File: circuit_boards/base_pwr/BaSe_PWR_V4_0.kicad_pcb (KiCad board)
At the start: 4 copper layers, 114.2 x 101.5 mm, 103 parts, among them J1 12VDC In, J10 Conn_01x04_Socket, J11 MOTOR, J12 USB3_A, J3 USB_B_Micro, J4 Conn_01x07_Pin, J5 Conn_02x06_Odd_Even, J6 USB3_B_Micro, J7 Conn_02x06_Odd_Even, J8 USB_C_Receptacle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

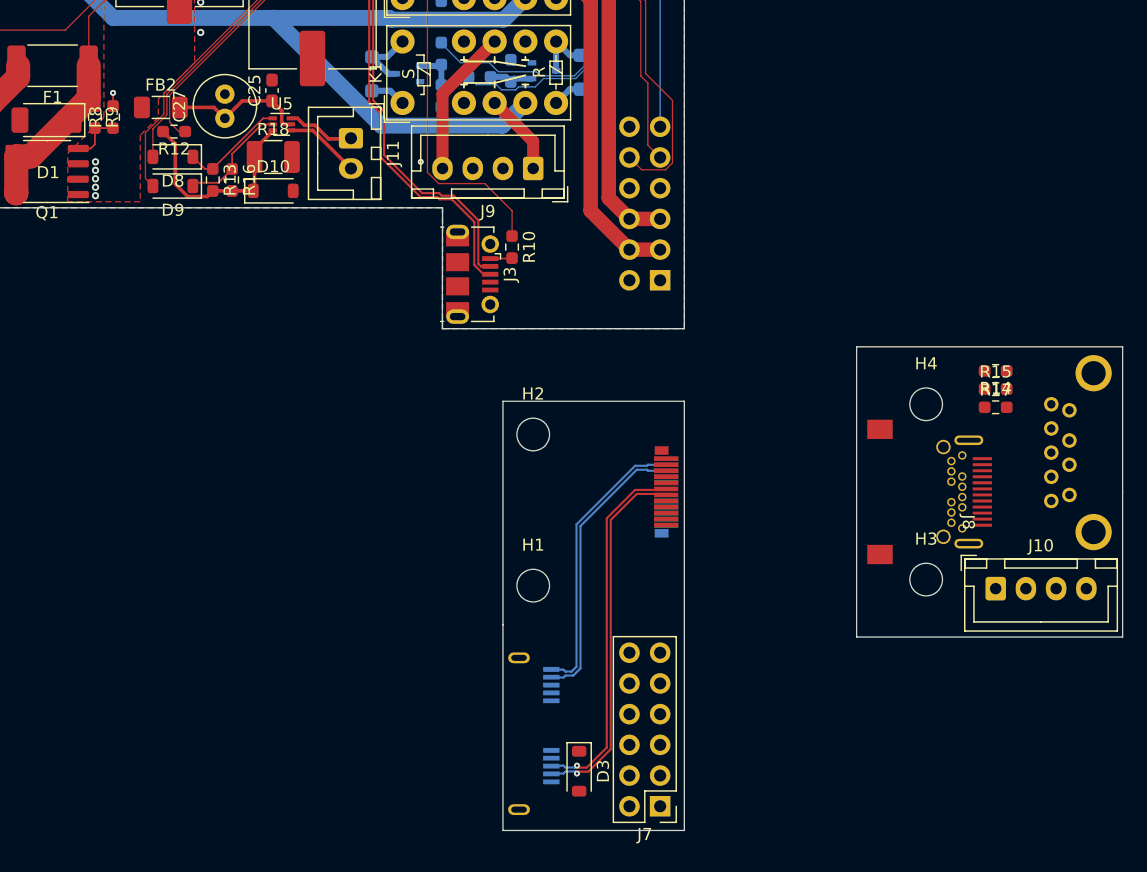
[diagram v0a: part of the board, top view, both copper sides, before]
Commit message: BaSe PWR V4.0: rotate b2b connectors 180 degree for shorter pwr tracks
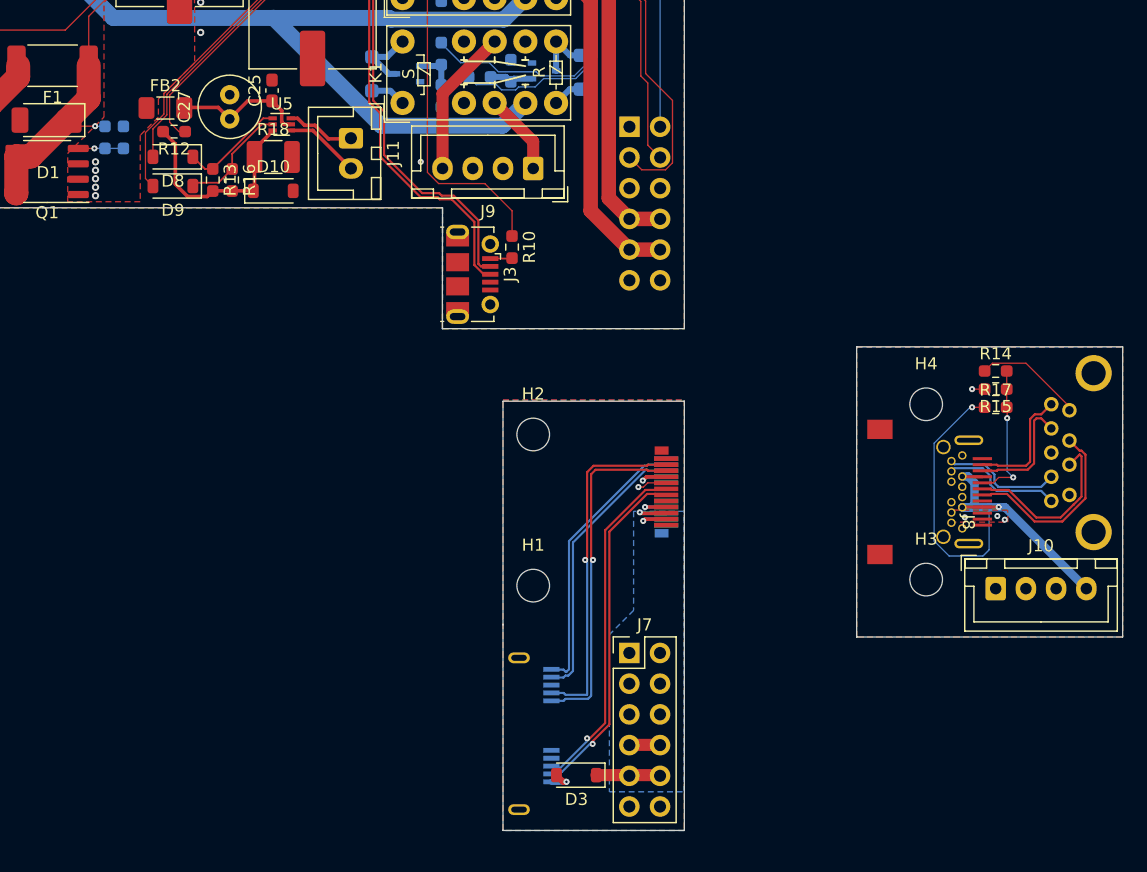
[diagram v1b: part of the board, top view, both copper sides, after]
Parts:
- R8, R9: moved to B.Cu
- moved J5 13.0 mm to (93.5, 106.8), turned to 180 degrees
- moved J7 12.9 mm to (93.5, 150.3), turned to 0 degrees
- moved R8 1.89 mm to (51.6, 107.7)
- moved R9 1.87 mm to (50.1, 107.7)
- moved C27 0.40 mm to (60.4, 106.2)
- moved D3 0.40 mm to (89.1, 160.4), turned to 180 degrees
- moved FB2 0.38 mm to (55.1, 105.2)
- turned R14 to 0 degrees
- turned R15 to 180 degrees
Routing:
- net +12VA: track 0.00 -> 44.1 mm, vias 0 -> 2
- net /stator_tx+: track 0.00 -> 28.3 mm, vias 0 -> 1
- net /stator_tx-: track 0.00 -> 28.3 mm, vias 0 -> 1
- net /lane1_d-: track 0.00 -> 15.7 mm
- net /lane1_d+: track 0.00 -> 14.6 mm
- net /+5V_HDD_: track 0.00 -> 13.7 mm, vias 0 -> 2
- net /supply_sense: track 0.00 -> 11.8 mm, vias 0 -> 2
- net /l1_tx-: track 0.00 -> 9.91 mm
- net /l1_tx+: track 0.00 -> 9.91 mm
- net /l1_rx-: track 0.00 -> 9.91 mm
- net /l1_rx+: track 0.00 -> 9.91 mm
- net +5VA: track 0.00 -> 9.07 mm, vias 0 -> 3
- net /+12V_HDD_: track 0.00 -> 8.92 mm, vias 0 -> 2
- net /DC_preprot: track 55.3 -> 59.1 mm, vias 1 -> 2
- net GND1: track 0.00 -> 2.54 mm
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- added copper zone on F.Cu, net +5VA
- added copper zone on In2.Cu, net +5VA
- added copper zone on In2.Cu, net /+12V_HDD_
- added copper zone on B.Cu, net /+5V_HDD_
- added copper zone on B.Cu, net GND1
- added copper zone on F.Cu, net GND1
- added copper zone on In1.Cu, net GND1
- added copper zone on In2.Cu, net GND1
- added copper zone on B.Cu, net GND2
- added copper zone on F.Cu, net GND2
- added copper zone on In1.Cu, net GND2
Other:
- board text added: "BaSe HW 4"

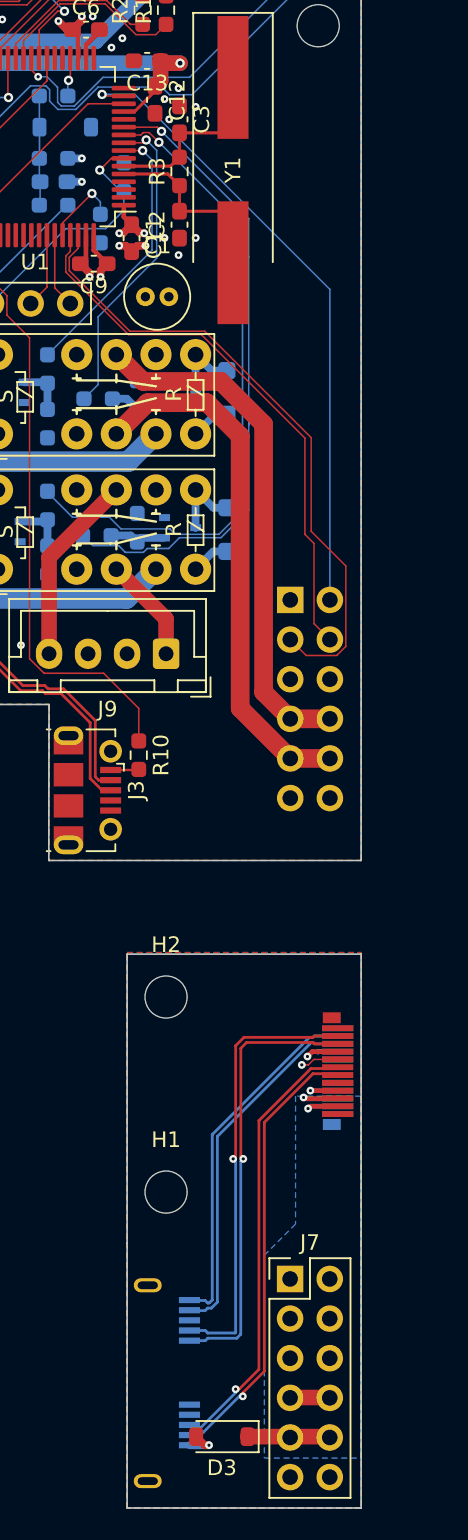
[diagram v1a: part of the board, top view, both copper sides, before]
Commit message: Base PWR V4.0: optimize pinout for b2b connectors
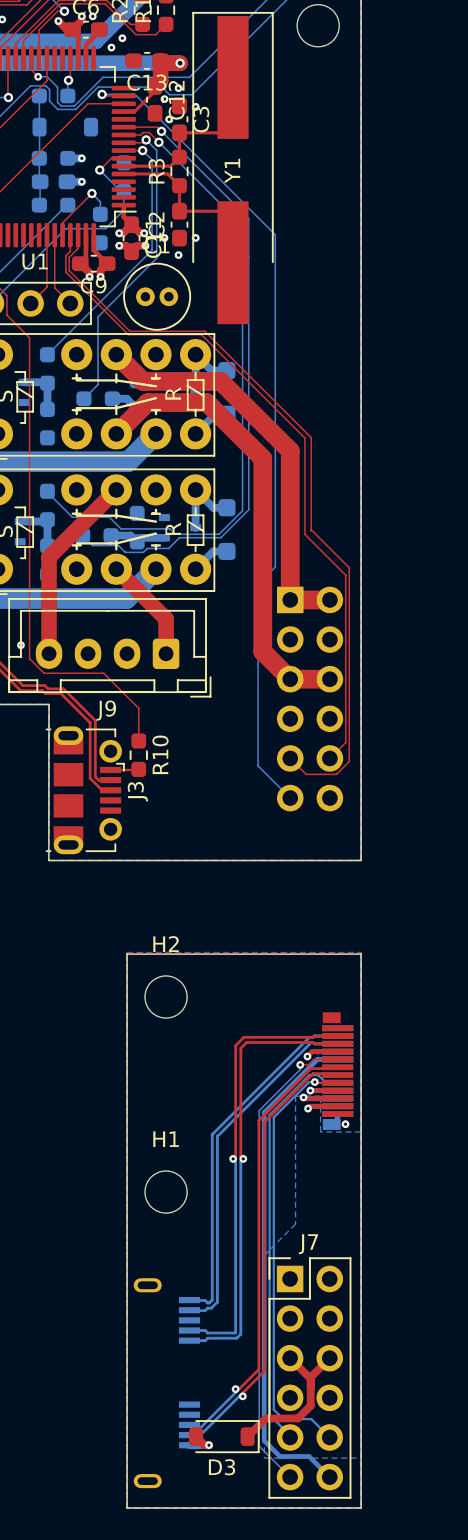
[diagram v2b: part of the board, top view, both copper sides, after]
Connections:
- J5 pad 1: GND -> /+12V_HDD
- J5 pad 10: /i2c1_sda -> /i2c1_scl
- J5 pad 2: GND -> /+12V_HDD
- J5 pad 3: /+5V_HDD -> GND
- J5 pad 4: /+5V_HDD -> GND
- J5 pad 5: /+12V_HDD -> /+5V_HDD
- J5 pad 6: /+12V_HDD -> /+5V_HDD
- J5 pad 9: /i2c1_scl -> /i2c1_sda
- J7 pad 1: GND1 -> /+12V_HDD_
- J7 pad 10: /i2c_sda -> /aux_i2c_scl
- J7 pad 2: GND1 -> /+12V_HDD_
- J7 pad 3: /+5V_HDD_ -> GND1
- J7 pad 4: /+5V_HDD_ -> GND1
- J7 pad 5: /+12V_HDD_ -> /+5V_HDD_
- J7 pad 6: /+12V_HDD_ -> /+5V_HDD_
- J7 pad 9: /i2c_scl -> /aux_i2c_sda
- P1 pad B5: /aux_3v3 -> /aux_i2c_sda
- P1 pad B8: /aux_i2c_sda -> /aux_3v3
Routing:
- net /aux_3v3: track 0.00 -> 33.1 mm
- net /stator_supply_sense_: track 2.44 -> 30.9 mm
- net /aux_i2c_scl: track 0.00 -> 28.2 mm, vias 0 -> 1
- net /aux_i2c_sda: track 0.00 -> 26.8 mm
- net /stator_supply_sense: track 41.1 -> 53.7 mm
- net /i2c1_scl: track 35.8 -> 44.3 mm
- net /i2c1_sda: track 41.0 -> 48.9 mm
- net /+12V_HDD: track 33.4 -> 25.8 mm
- net /+5V_HDD_: track 13.7 -> 19.2 mm
- net /+5V_HDD: track 34.2 -> 29.1 mm
- net GND1: track 2.54 -> 0.83 mm, vias 0 -> 1

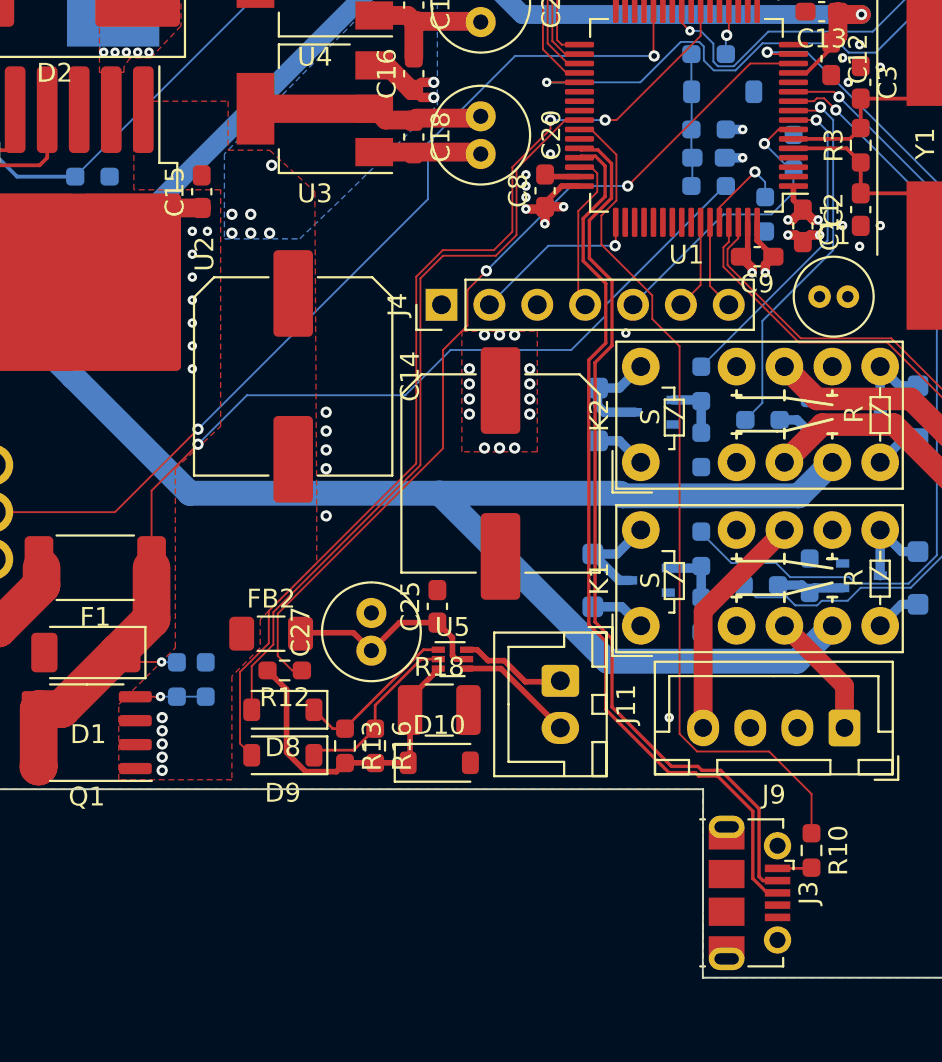
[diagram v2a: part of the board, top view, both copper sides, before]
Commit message: BaSe PWR V4.0: resolve DRC errors
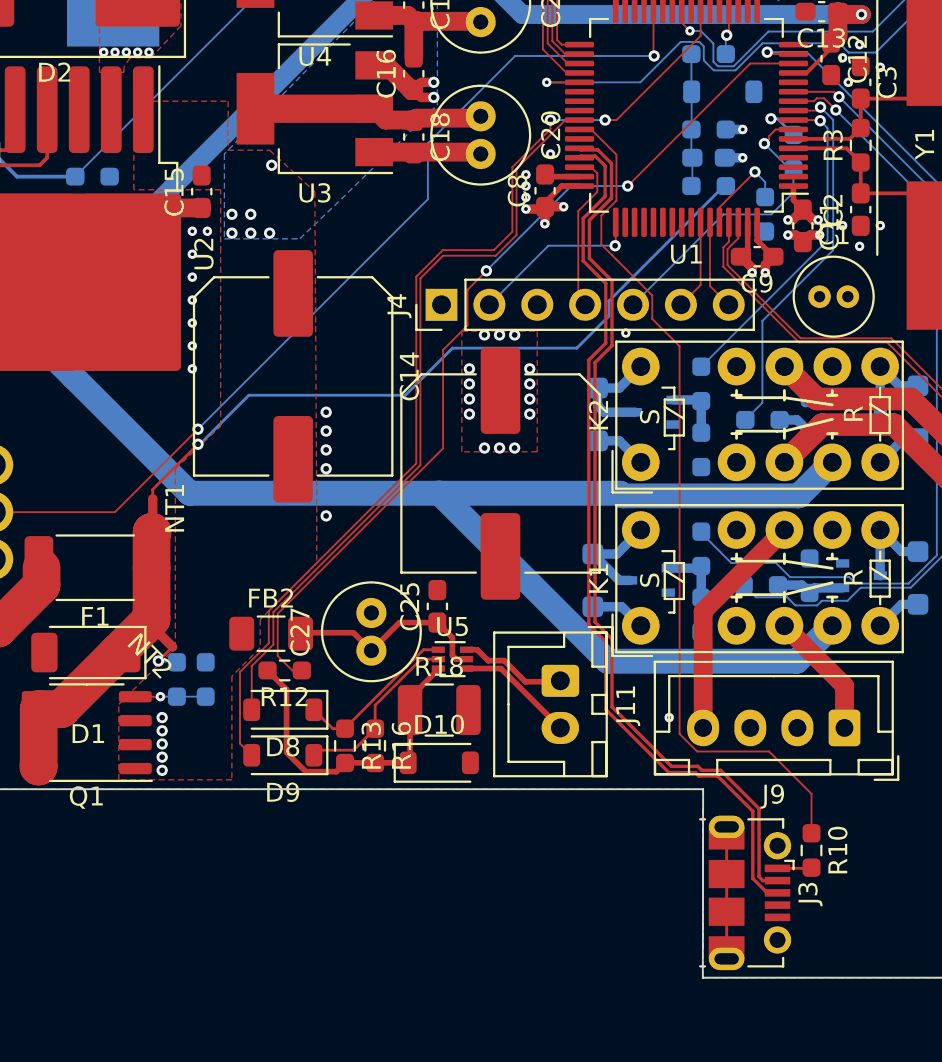
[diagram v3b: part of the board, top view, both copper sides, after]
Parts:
- added NT1: NetTie_2, NetTie:NetTie-2_SMD_Pad0.5mm, F.Cu at (48.8, 98.6)
- added NT2: NetTie_2, NetTie:NetTie-2_SMD_Pad0.5mm, F.Cu at (49.5, 105.6)
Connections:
- R6 pad 2: /DC_preprot -> Net-(NT1-Pad1)
- R9 pad 1: /DC_preprot -> Net-(NT2-Pad1)
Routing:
- net /DC_preprot: track 59.1 -> 17.3 mm, vias 2 -> 0
- net Net-(NT1-Pad1): track 0.00 -> 38.0 mm, vias 0 -> 1
- net GND: track 38.2 -> 44.6 mm
- net Net-(NT2-Pad1): track 0.00 -> 2.13 mm, vias 0 -> 1
- net +3V3_STBY: track 32.0 -> 33.5 mm, vias 9 -> 10

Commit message: BaSe PWR V4.0: production ready
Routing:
- net /DC_preprot: track 17.3 -> 15.7 mm
- net /+12V_HDD_: track 8.92 -> 7.63 mm
- net /aux_3v3: track 33.1 -> 32.3 mm
- net GND2: vias 1 -> 94
- net GND1: vias 1 -> 87
- net GND: vias 60 -> 348

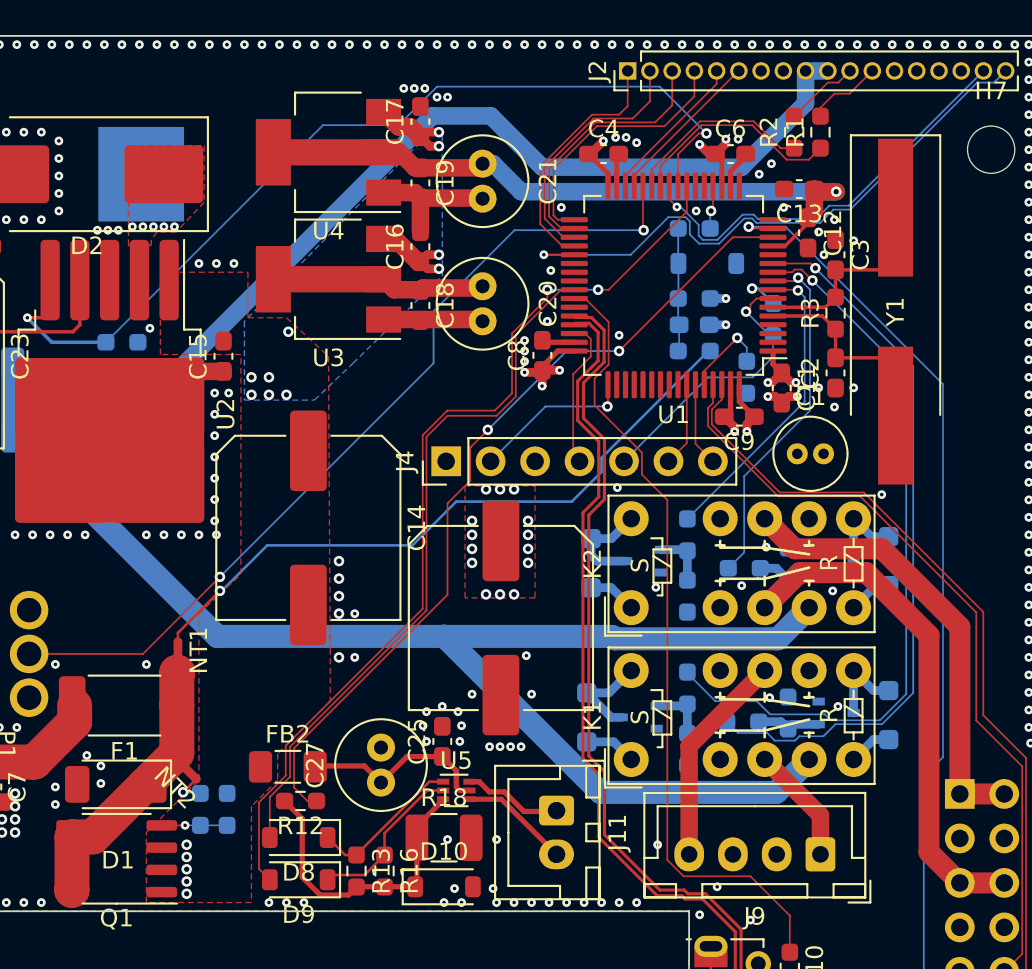
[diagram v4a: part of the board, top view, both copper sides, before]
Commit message: BaSe_PWR_V4_0: add stitching vias
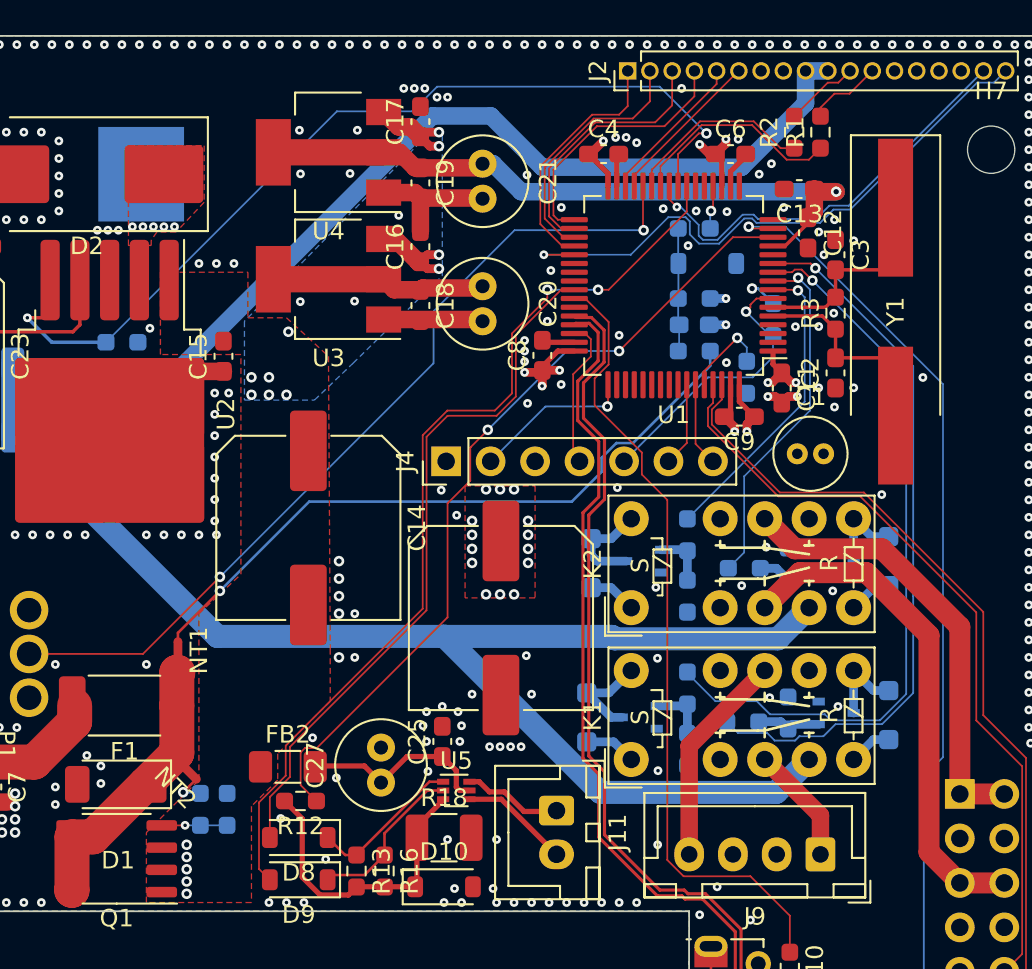
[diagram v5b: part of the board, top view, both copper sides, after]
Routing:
- net GND: vias 348 -> 376
